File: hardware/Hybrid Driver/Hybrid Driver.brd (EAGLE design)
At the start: 55.9 x 76.2 mm, 35 parts, among them CN1 MTA100-6, CN2 SE14, U1 M57962L, U2 VLA106-15242, U3 M57962L, U4 VLA106-15242

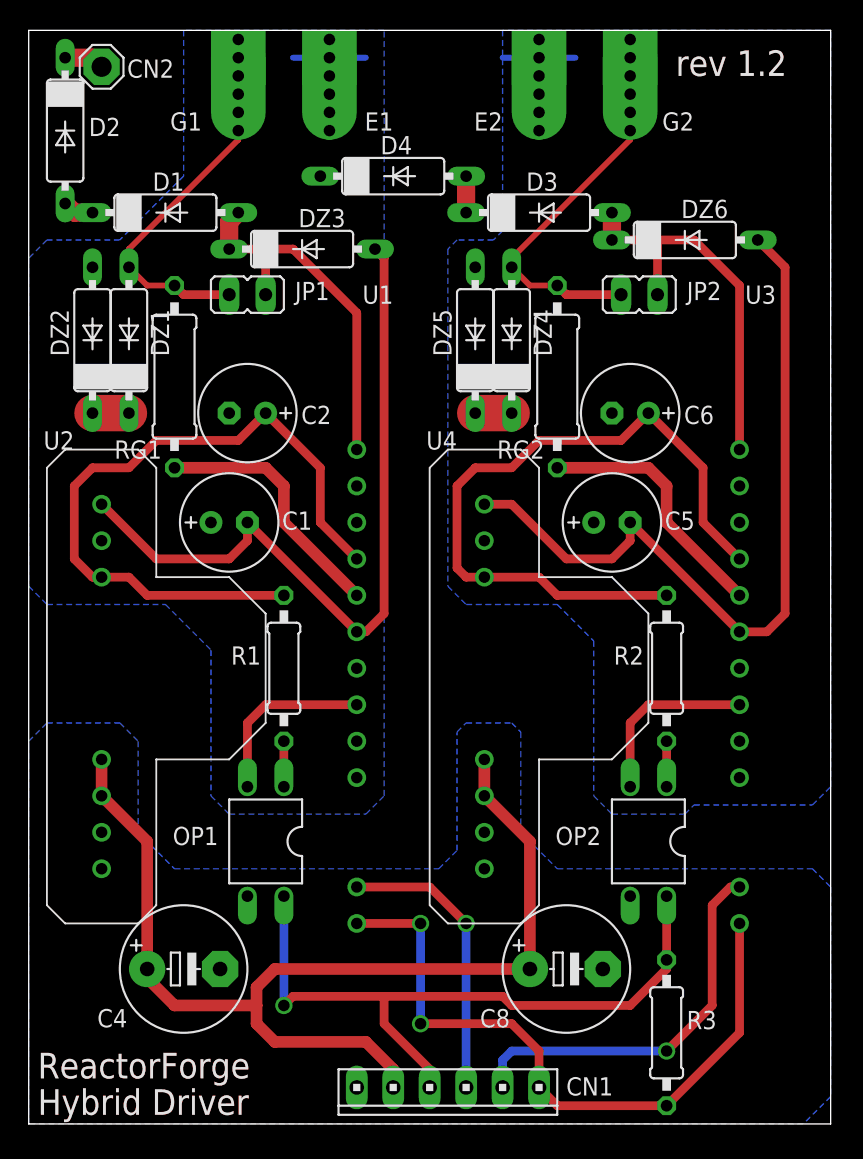
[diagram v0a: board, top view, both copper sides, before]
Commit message: reduced board width to 2 inches, added decoupling cap on 5V supply, updated documentation and library components
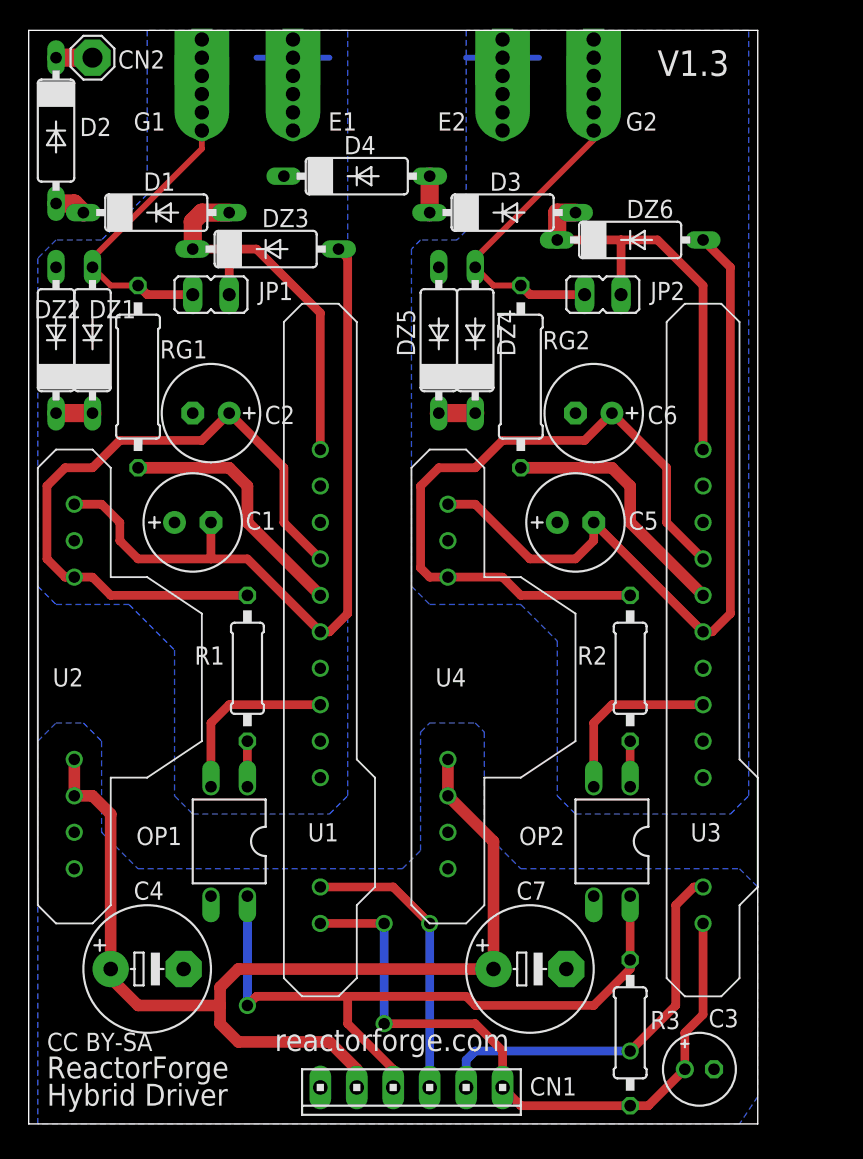
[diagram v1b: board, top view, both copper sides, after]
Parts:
- removed C8: 150uF, resistor:E5-8,5
- added C3: 10uF, rcl:E2-5
- added C7: 150uF, resistor:E5-8,5
- JP1, JP2: value (none) -> 0
- RG1, RG2: value (none) -> 3
- moved DZ6 3.81 mm to (41.9, 61.6)
- moved R2 2.54 mm to (41.9, 31.8)
- moved R3 2.54 mm to (41.9, 6.35)
- moved DZ4 2.54 mm to (31.1, 54.6)
- moved U4 2.54 mm to (25.4, 47.0)
- moved C1 2.54 mm to (11.4, 41.9)
- moved C2 2.54 mm to (12.7, 49.5)
- moved G1 2.54 mm to (12.1, 70.5)
- moved JP1 2.54 mm to (12.7, 57.8)
- moved OP1 2.54 mm to (14.0, 19.7)
- moved R1 2.54 mm to (15.2, 31.8)
- moved DZ1 2.54 mm to (4.45, 54.6)
- moved DZ2 2.54 mm to (1.91, 54.6)
- moved RG1 2.54 mm to (7.62, 52.1)
- moved C4 2.54 mm to (8.26, 10.8)
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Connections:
- net GND: now also C3.-, C7.-; no longer C8.-
- net N$30: now also C7.+; no longer C8.+
- net N$9: now also C3.+
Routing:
- net N$22: track 27.4 -> 29.9 mm
- net N$4: track 26.2 -> 28.1 mm
- net N$14: track 54.8 -> 53.6 mm
- net N$16: track 49.0 -> 47.7 mm
- net N$9: track 47.2 -> 48.0 mm
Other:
- board size 55.9 x 76.2 mm -> 50.8 x 76.2 mm
- board text added: "CC BY-SA"
- board text added: "V1.3"
- board text added: "reactorforge.com"
- board text removed: "rev 1.2"

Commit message: added OSH logo, tweaked silkscreen
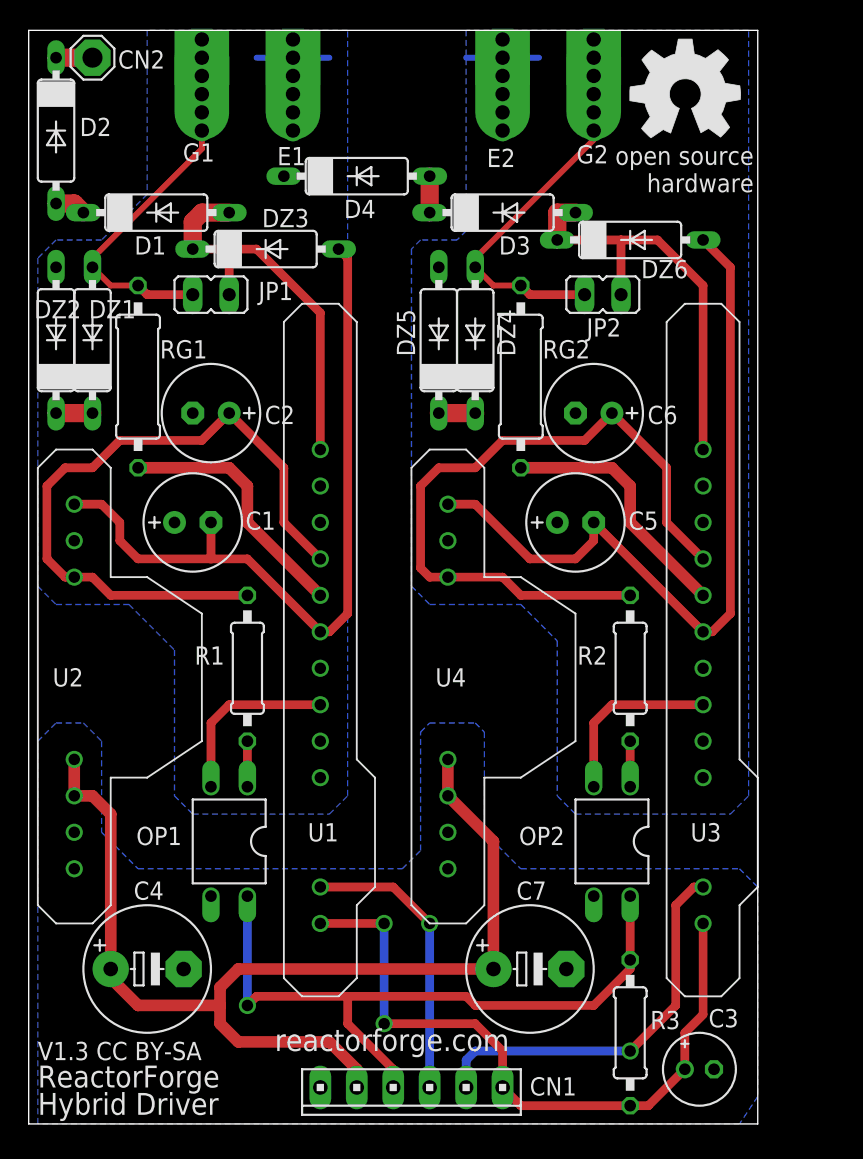
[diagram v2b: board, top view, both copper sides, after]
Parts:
- added GOLD_ORB_SM1: OSHWLOGOLOGO8MM, oshw:OSHW_8MM
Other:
- board text added: "F"
- board text added: "R"
- board text added: "V1.3 CC BY-SA"
- board text removed: "CC BY-SA"
- board text removed: "V1.3"
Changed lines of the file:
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@@
 <layer number="54" name="bGND_GNDA" color="7" fill="1" visible="no" active="no"/>
 <layer number="56" name="wert" color="7" fill="1" visible="no" active="no"/>
+<layer number="90" name="Modules" color="5" fill="1" visible="no" active="no"/>
 <layer number="91" name="Nets" color="2" fill="1" visible="no" active="no"/>
 <layer number="92" name="Busses" color="1" fill="1" visible="no" active="no"/>
@@
 <layer number="121" name="_tsilk" color="7" fill="1" visible="yes" active="yes"/>
 <layer number="122" name="_bsilk" color="7" fill="1" visible="yes" active="yes"/>
+<layer number="125" name="_tNames" color="7" fill="1" visible="yes" active="yes"/>
 <layer number="131" name="prix" color="7" fill="1" visible="yes" active="yes"/>
 <layer number="132" name="test" color="7" fill="1" visible="yes" active="yes"/>
+<layer number="144" name="Drill_legend" color="7" fill="1" visible="yes" active="yes"/>
 <layer number="151" name="HeatSink" color="7" fill="1" visible="yes" active="yes"/>
 <layer number="200" name="200bmp" color="7" fill="1" visible="yes" active="yes"/>
@@
 <layer number="207" name="207bmp" color="7" fill="1" visible="yes" active="yes"/>
 <layer number="208" name="208bmp" color="7" fill="1" visible="yes" active="yes"/>
+<layer number="209" name="209bmp" color="7" fill="1" visible="yes" active="yes"/>
+<layer number="210" name="210bmp" color="7" fill="1" visible="yes" active="yes"/>
+<layer number="211" name="211bmp" color="7" fill="1" visible="yes" active="yes"/>
+<layer number="212" name="212bmp" color="7" fill="1" visible="yes" active="yes"/>
+<layer number="213" name="213bmp" color="7" fill="1" visible="yes" active="yes"/>
+<layer number="214" name="214bmp" color="7" fill="1" visible="yes" active="yes"/>
+<layer number="215" name="215bmp" color="7" fill="1" visible="yes" active="yes"/>
+<layer number="216" name="216bmp" color="7" fill="1" visible="yes" active="yes"/>
 <layer number="250" name="Descript" color="7" fill="1" visible="yes" active="yes"/>
 <layer number="251" name="SMDround" color="7" fill="1" visible="yes" active="yes"/>
@@
 <wire x1="50.8" y1="76.2" x2="0" y2="76.2" width="0" layer="20"/>
 <wire x1="0" y1="76.2" x2="0" y2="0" width="0" layer="20"/>
-<text x="43.815" y="73.025" size="1.778" layer="21" font="vector" ratio="15">V1.3</text>
-<text x="1.27" y="3.175" size="1.524" layer="21" font="vector" ratio="15">ReactorForge</text>
-<text x="1.27" y="1.27" size="1.524" layer="21" font="vector" ratio="15">Hybrid Driver</text>
+<text x="0.635" y="2.54" size="1.524" layer="21" font="vector" ratio="15">ReactorForge</text>
+<text x="0.635" y="0.635" size="1.524" layer="21" font="vector" ratio="15">Hybrid Driver</text>
 <text x="36.83" y="5.08" size="1.524" layer="22" font="vector" ratio="15" rot="MR0">reactorforge.com</text>
 <text x="17.145" y="5.08" size="1.524" layer="21" font="vector" ratio="15">reactorforge.com</text>
-<text x="1.27" y="5.08" size="1.27" layer="21" font="vector" ratio="15">CC BY-SA</text>
+<text x="0.635" y="4.445" size="1.27" layer="21" font="vector" ratio="15">V1.3 CC BY-SA</text>
+<text x="43.307" y="70.866" size="1.778" layer="1" font="vector" ratio="15">R</text>
+<text x="47.117" y="70.866" size="1.778" layer="1" font="vector" ratio="15">F</text>
 </plain>
 <attributes>
@@
 </element>
 <element name="RG2" library="resistor" package="0309/12" value="3" x="34.29" y="52.07" smashed="yes" rot="R90">
-<attribute name="NAME" x="35.814" y="53.975" size="1.27" layer="25" ratio="10"/>
+<attribute name="NAME" x="35.814" y="53.34" size="1.27" layer="25" ratio="10"/>
 <attribute name="VALUE" x="34.9758" y="48.895" size="1.27" layer="27" ratio="10" rot="R90"/>
 </element>
@@
 </element>
 <element name="D1" library="diode" package="DO07" value="MUR1100E" x="8.89" y="63.5" smashed="yes">
-<attribute name="NAME" x="8.001" y="65.024" size="1.27" layer="25" ratio="10"/>
+<attribute name="NAME" x="7.366" y="60.579" size="1.27" layer="25" ratio="10"/>
 <attribute name="VALUE" x="5.461" y="60.579" size="1.27" layer="27" ratio="10"/>
 </element>
@@
 </element>
 <element name="D3" library="diode" package="DO07" value="MUR1100E" x="33.02" y="63.5" smashed="yes">
-<attribute name="NAME" x="32.131" y="65.024" size="1.27" layer="25" ratio="10"/>
+<attribute name="NAME" x="32.766" y="60.579" size="1.27" layer="25" ratio="10"/>
 <attribute name="VALUE" x="29.591" y="60.579" size="1.27" layer="27" ratio="10"/>
 </element>
 <element name="D4" library="diode" package="DO07" value="MUR1100E" x="22.86" y="66.04" smashed="yes">
-<attribute name="NAME" x="21.971" y="67.564" size="1.27" layer="25" ratio="10"/>
+<attribute name="NAME" x="21.971" y="63.119" size="1.27" layer="25" ratio="10"/>
 </element>
 <element name="DZ2" library="1-Custom" package="DIODE.4-AXIAL" value="1N4745" x="1.905" y="54.61" smashed="yes" rot="R90">
@@
 </element>
 <element name="DZ6" library="1-Custom" package="DIODE.4-AXIAL" value="1N4751" x="41.91" y="61.595" smashed="yes">
-<attribute name="NAME" x="41.656" y="63.119" size="1.27" layer="25" ratio="10"/>
+<attribute name="NAME" x="42.672" y="58.928" size="1.27" layer="25" ratio="10"/>
 <attribute name="VALUE" x="38.481" y="58.674" size="1.27" layer="27" ratio="10"/>
 </element>
@@
 </element>
 <element name="JP2" library="jumper" package="JP1" value="0" x="40.005" y="57.785" smashed="yes" rot="R90">
-<attribute name="NAME" x="45.72" y="58.674" size="1.27" layer="25" ratio="10" rot="R180"/>
+<attribute name="NAME" x="41.275" y="56.134" size="1.27" layer="25" ratio="10" rot="R180"/>
 <attribute name="VALUE" x="42.545" y="60.706" size="1.27" layer="27" ratio="10" rot="R180"/>
 </element>
 <element name="G1" library="1-Custom" package="IGBT-PAD" value="IGBT-PAD" x="12.065" y="70.485" smashed="yes">
-<attribute name="NAME" x="9.525" y="70.485" size="1.27" layer="25" rot="R180"/>
+<attribute name="NAME" x="12.954" y="68.326" size="1.27" layer="25" rot="R180"/>
 </element>
 <element name="E1" library="1-Custom" package="IGBT-PAD" value="IGBT-PAD" x="18.415" y="70.485" smashed="yes">
-<attribute name="NAME" x="22.86" y="70.485" size="1.27" layer="25" rot="R180"/>
+<attribute name="NAME" x="19.304" y="68.072" size="1.27" layer="25" rot="R180"/>
 </element>
 <element name="G2" library="1-Custom" package="IGBT-PAD" value="IGBT-PAD" x="39.37" y="70.485" smashed="yes">
-<attribute name="NAME" x="43.815" y="70.485" size="1.27" layer="25" rot="R180"/>
+<attribute name="NAME" x="40.386" y="68.199" size="1.27" layer="25" rot="R180"/>
 </element>
 <element name="E2" library="1-Custom" package="IGBT-PAD" value="IGBT-PAD" x="33.02" y="70.485" smashed="yes">
-<attribute name="NAME" x="30.48" y="70.485" size="1.27" layer="25" rot="R180"/>
+<attribute name="NAME" x="33.909" y="67.945" size="1.27" layer="25" rot="R180"/>
 </element>
 <element name="C3" library="rcl" library_urn="urn:adsk.eagle:library:334" package="E2-5" package3d_urn="urn:adsk.eagle:package:23346/2" value="10uF" x="46.736" y="3.81" smashed="yes">
@@
 <attribute name="VALUE" x="49.276" y="1.651" size="1.27" layer="27" ratio="10"/>
 </element>
+<element name="GOLD_ORB_SM1" library="oshw" package="OSHW_8MM" value="OSHWLOGOLOGO8MM" x="45.72" y="71.755"/>
 </elements>
 <signals>
@@
 </drawing>
 <compatibility>
+<note version="6.3" minversion="6.2.2" severity="warning">
+Since Version 6.2.2 text objects can contain more than one line,
+which will not be processed correctly with this version.
+</note>
 <note version="8.2" severity="warning">
 Since Version 8.2, EAGLE supports online libraries. The ids

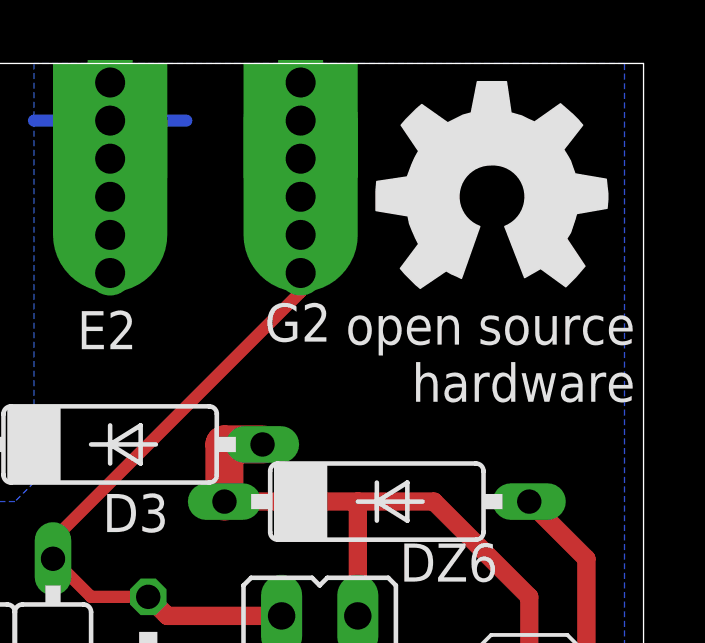
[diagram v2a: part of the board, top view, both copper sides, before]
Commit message: moved OSH logo down, added board renderings
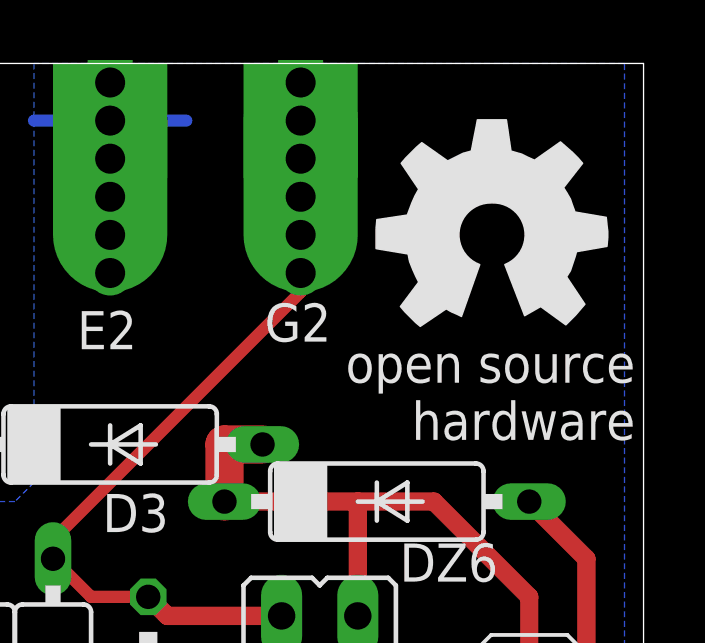
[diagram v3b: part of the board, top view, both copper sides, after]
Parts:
- moved GOLD_ORB_SM1 1.27 mm to (45.7, 70.5)
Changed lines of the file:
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@@
 <text x="17.145" y="5.08" size="1.524" layer="21" font="vector" ratio="15">reactorforge.com</text>
 <text x="0.635" y="4.445" size="1.27" layer="21" font="vector" ratio="15">V1.3 CC BY-SA</text>
-<text x="43.307" y="70.866" size="1.778" layer="1" font="vector" ratio="15">R</text>
-<text x="47.117" y="70.866" size="1.778" layer="1" font="vector" ratio="15">F</text>
+<text x="43.307" y="69.596" size="1.778" layer="1" font="vector" ratio="15">R</text>
+<text x="47.117" y="69.596" size="1.778" layer="1" font="vector" ratio="15">F</text>
 </plain>
 <attributes>
@@
 <attribute name="VALUE" x="49.276" y="1.651" size="1.27" layer="27" ratio="10"/>
 </element>
-<element name="GOLD_ORB_SM1" library="oshw" package="OSHW_8MM" value="OSHWLOGOLOGO8MM" x="45.72" y="71.755"/>
+<element name="GOLD_ORB_SM1" library="oshw" package="OSHW_8MM" value="OSHWLOGOLOGO8MM" x="45.72" y="70.485"/>
 </elements>
 <signals>
